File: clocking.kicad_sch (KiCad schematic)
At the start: 2 parts, among them U12 LMX2594, U18 LMK0482x

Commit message: Renumber refdes
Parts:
- removed U12: LMX2594, Package_DFN_QFN:VQFN-40-1EP_5x5mm_P0.4mm_EP3.3x3.3mm, symbol huskylib:LMX2594
- removed U18: LMK0482x, Package_DFN_QFN:QFN-64-1EP_9x9mm_P0.5mm_EP4.7x4.7mm_ThermalVias, symbol huskylib:LMK0482x

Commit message: Add lmk and bump schematic size
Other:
- added sheet LMK04828 (lmk04828.kicad_sch)
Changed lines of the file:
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@@
 	(generator "eeschema")
 	(generator_version "9.0")
-	(paper "A4")
+	(paper "A3")
+	(sheet
+		(at 54.61 50.8)
+		(size 62.23 43.18)
+		(exclude_from_sim no)
+		(in_bom yes)
+		(on_board yes)
+		(dnp no)
+		(fields_autoplaced yes)
+		(stroke
+			(width 0.1524)
+			(type solid)
+		)
+		(fill
+			(color 0 0 0 0.0000)
+		)
+		(property "Sheetname" "LMK04828"
+			(at 54.61 50.0884 0)
+			(effects
+				(font
+					(size 1.27 1.27)
+				)
+				(justify left bottom)
+			)
+		)
+		(property "Sheetfile" "lmk04828.kicad_sch"
+			(at 54.61 94.5646 0)
+			(effects
+				(font
+					(size 1.27 1.27)
+				)
+				(justify left top)
+			)
+		)
+		(instances
+			(project "huskypointofload"
+				(path "/eb9c972b-d134-41da-be97-ece3f463f7e0/d5a7e3c4-49dd-4cc7-9d82-7c02320e6daf"
+					(page "17")
+				)
+			)
+		)
+	)
 )

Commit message: Complete LMK schematic
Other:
- sheet LMK04828 ports: added BACKUP_DIS, DCLK0n, DCLK0p, LD1, LD2, RESET, SCK, SDCLK1n, SDCLK1p, SDIO, SEL0, SEL1, ~{CS}; removed none
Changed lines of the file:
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@@
 	(sheet
 		(at 54.61 50.8)
-		(size 62.23 43.18)
+		(size 29.21 30.48)
 		(exclude_from_sim no)
 		(in_bom yes)
@@
 		)
 		(property "Sheetfile" "lmk04828.kicad_sch"
-			(at 54.61 94.5646 0)
+			(at 54.61 81.8646 0)
 			(effects
 				(font
@@
 			)
 		)
+		(pin "BACKUP_DIS" input
+			(at 54.61 53.34 180)
+			(effects
+				(font
+					(size 1.27 1.27)
+				)
+				(justify left)
+			)
+		)
+		(pin "DCLK0n" input
+			(at 83.82 55.88 0)
+			(effects
+				(font
+					(size 1.27 1.27)
+				)
+				(justify right)
+			)
+		)
+		(pin "DCLK0p" input
+			(at 83.82 53.34 0)
+			(effects
+				(font
+					(size 1.27 1.27)
+				)
+				(justify right)
+			)
+		)
+		(pin "LD1" input
+			(at 54.61 76.2 180)
+			(effects
+				(font
+					(size 1.27 1.27)
+				)
+				(justify left)
+			)
+		)
+		(pin "LD2" input
+			(at 54.61 78.74 180)
+			(effects
+				(font
+					(size 1.27 1.27)
+				)
+				(justify left)
+			)
+		)
+		(pin "RESET" input
+			(at 54.61 55.88 180)
+			(effects
+				(font
+					(size 1.27 1.27)
+				)
+				(justify left)
+			)
+		)
+		(pin "SCK" input
+			(at 54.61 63.5 180)
+			(effects
+				(font
+					(size 1.27 1.27)
+				)
+				(justify left)
+			)
+		)
+		(pin "SDCLK1n" input
+			(at 83.82 63.5 0)
+			(effects
+				(font
+					(size 1.27 1.27)
+				)
+				(justify right)
+			)
+		)
+		(pin "SDCLK1p" input
+			(at 83.82 60.96 0)
+			(effects
+				(font
+					(size 1.27 1.27)
+				)
+				(justify right)
+			)
+		)
+		(pin "SDIO" input
+			(at 54.61 66.04 180)
+			(effects
+				(font
+					(size 1.27 1.27)
+				)
+				(justify left)
+			)
+		)
+		(pin "SEL0" input
+			(at 54.61 71.12 180)
+			(effects
+				(font
+					(size 1.27 1.27)
+				)
+				(justify left)
+			)
+		)
+		(pin "SEL1" input
+			(at 54.61 73.66 180)
+			(effects
+				(font
+					(size 1.27 1.27)
+				)
+				(justify left)
+			)
+		)
+		(pin "~{CS}" input
+			(at 54.61 60.96 180)
+			(effects
+				(font
+					(size 1.27 1.27)
+				)
+				(justify left)
+			)
+		)

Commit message: Add LMX Draft
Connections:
- no-connect marks 0 -> 1
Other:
- added sheet LMX2594 (lmx2594.kicad_sch)

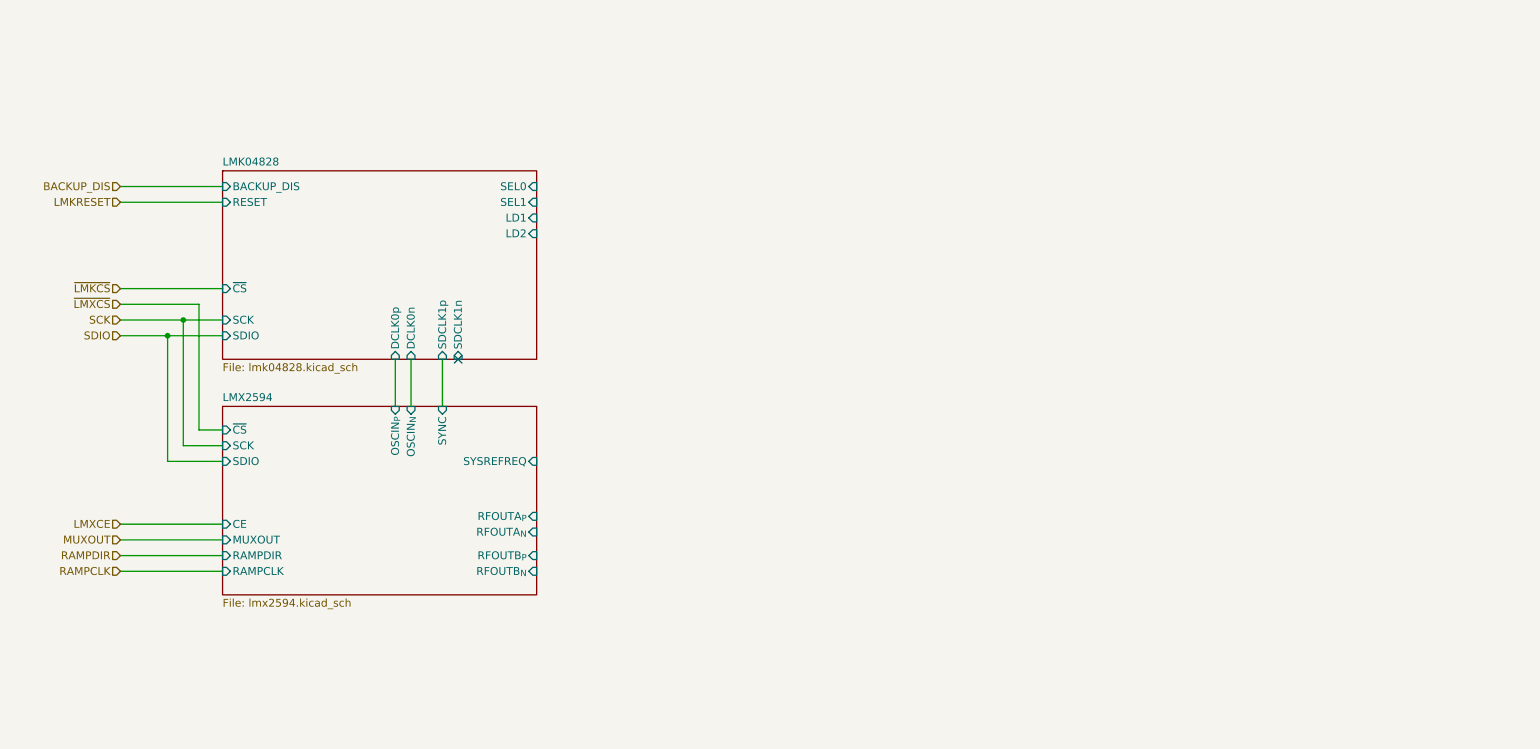
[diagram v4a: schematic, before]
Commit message: Different Matching Circuit
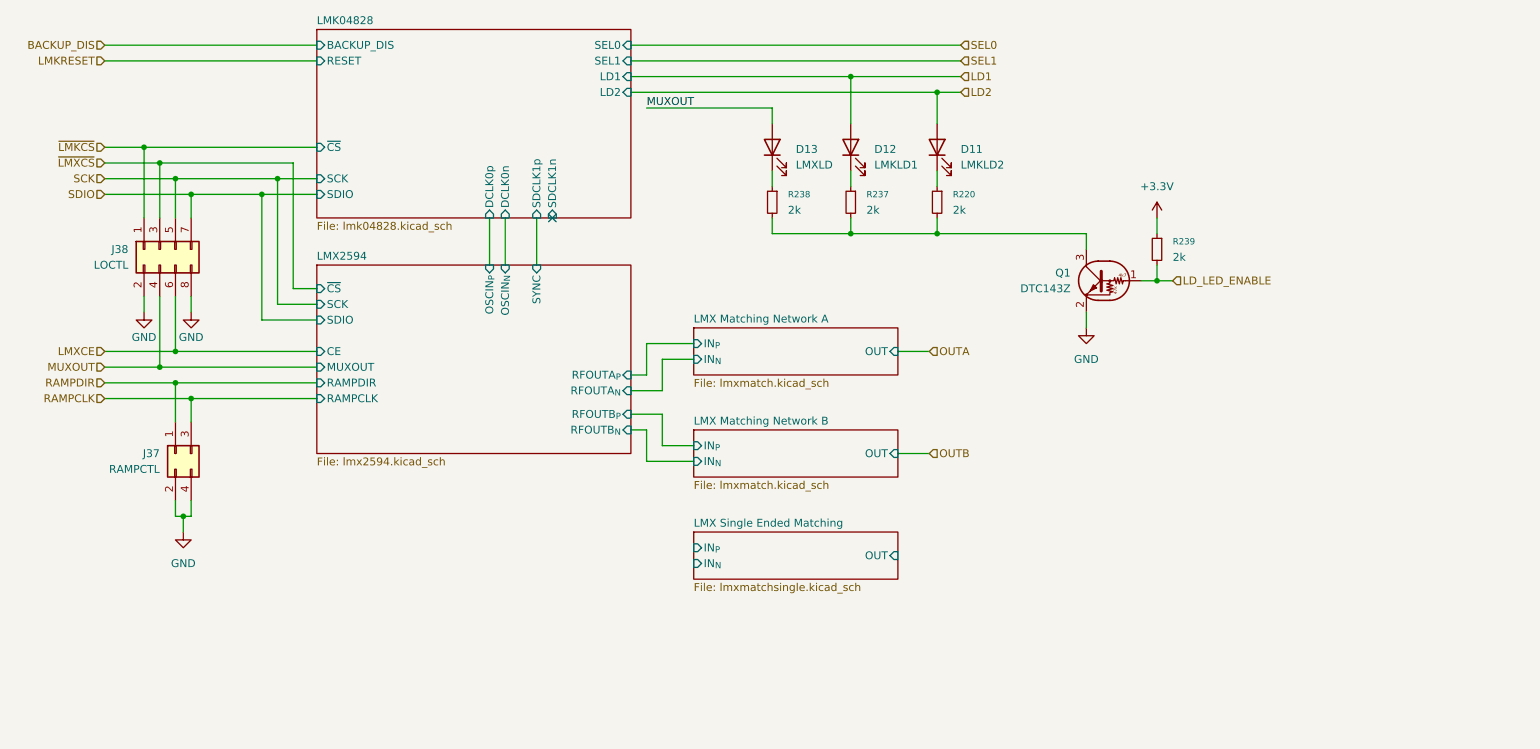
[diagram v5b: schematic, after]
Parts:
- added D11: LMKLD2, symbol Device:LED
- added D12: LMKLD1, symbol Device:LED
- added D13: LMXLD, symbol Device:LED
- added J37: RAMPCTL, symbol Connector_Generic:Conn_02x02_Odd_Even
- added J38: LOCTL, symbol Connector_Generic:Conn_02x04_Odd_Even
- added Q1: DTC143Z, symbol Transistor_BJT:DTC143Z
- added R220, R237, R238, R239: 2k, symbol Device:R_Small
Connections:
- net LMXCE: now also J38.6 (Pin_6)
- net MUXOUT: now also D13.2 (A), J38.4 (Pin_4)
- net RAMPCLK: now also J37.3 (Pin_3)
- net RAMPDIR: now also J37.1 (Pin_1)
- net SCK: now also J38.5 (Pin_5)
- net SDIO: now also J38.7 (Pin_7)
- net ~{LMKCS}: now also J38.1 (Pin_1)
- net ~{LMXCS}: now also J38.3 (Pin_3)
- new net: D13.1 (K), R238.1
- new net: Q1.3 (C), R220.2, R237.2, R238.2
- new net: D11.1 (K), R220.1
- new net: D12.1 (K), R237.1
- new net +3.3V: R239.1
- new net GND: J37.2 (Pin_2), J37.4 (Pin_4), J38.2 (Pin_2), J38.8 (Pin_8), Q1.2 (E)
- new net LD1: D12.2 (A)
- new net LD2: D11.2 (A)
- new net LD_LED_ENABLE: Q1.1 (B), R239.2
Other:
- added sheet LMX Matching Network A (lmxmatch.kicad_sch)
- added sheet LMX Matching Network B (lmxmatch.kicad_sch)
- added sheet LMX Single Ended Matching (lmxmatchsingle.kicad_sch)
- sheet LMX2594 ports: added none; removed SYSREFREQ

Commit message: Add mixer
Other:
- sheet LMX Single Ended Matching renamed LMX Single Ended Matching A
- removed sheet LMX Matching Network A
- removed sheet LMX Matching Network B
- added sheet LMX Single Ended Matching B (lmxmatchsingle.kicad_sch)
